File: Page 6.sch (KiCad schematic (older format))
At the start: 3 parts, among them U601 BME280

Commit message: Updates
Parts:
- C601, C602: Mftr Part No. (none) -> Yageo CC0603KPX7R7BB104
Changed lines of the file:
@@
 F 2 "Capacitor_SMD:C_0603_1608Metric_Pad1.05x0.95mm_HandSolder" H 7838 3700 50  0001 C CNN
 F 3 "https://www.yageo.com/upload/media/product/productsearch/datasheet/mlcc/UPY-GPHC_X7R_6.3V-to-50V_18.pdf" H 7800 3850 50  0001 C CNN
+F 4 "Yageo CC0603KPX7R7BB104" H 7800 3850 50  0001 C CNN "Mftr Part No."
 	1    7800 3850
 	1    0    0    -1
@@
 F 2 "Capacitor_SMD:C_0603_1608Metric_Pad1.05x0.95mm_HandSolder" H 7338 3700 50  0001 C CNN
 F 3 "https://www.yageo.com/upload/media/product/productsearch/datasheet/mlcc/UPY-GPHC_X7R_6.3V-to-50V_18.pdf" H 7300 3850 50  0001 C CNN
+F 4 "Yageo CC0603KPX7R7BB104" H 7300 3850 50  0001 C CNN "Mftr Part No."
 	1    7300 3850
 	1    0    0    -1

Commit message: Updates
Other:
- note added: "Environmental Sensor"
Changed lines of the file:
@@
 Wire Wire Line
 	7800 4000 7800 4650
+Text Notes 5750 5250 0    98   ~ 20
+Environmental Sensor
 $EndSCHEMATC

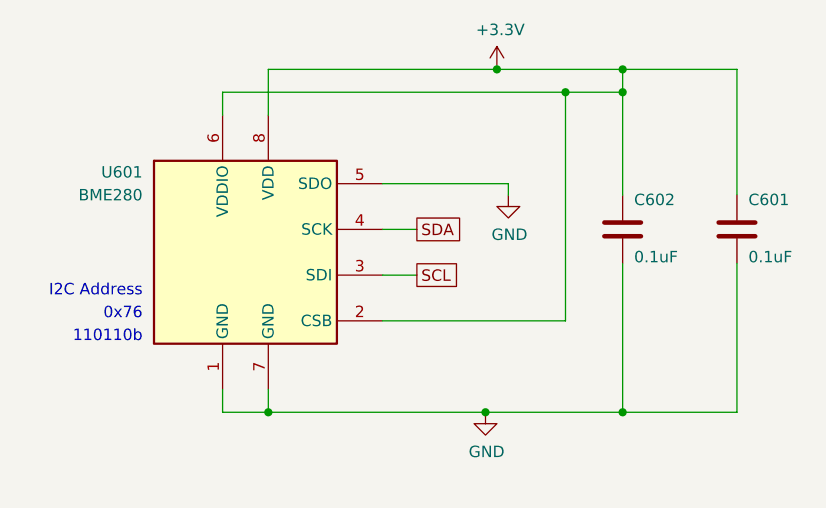
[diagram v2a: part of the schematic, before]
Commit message: Switched to Hierarchical
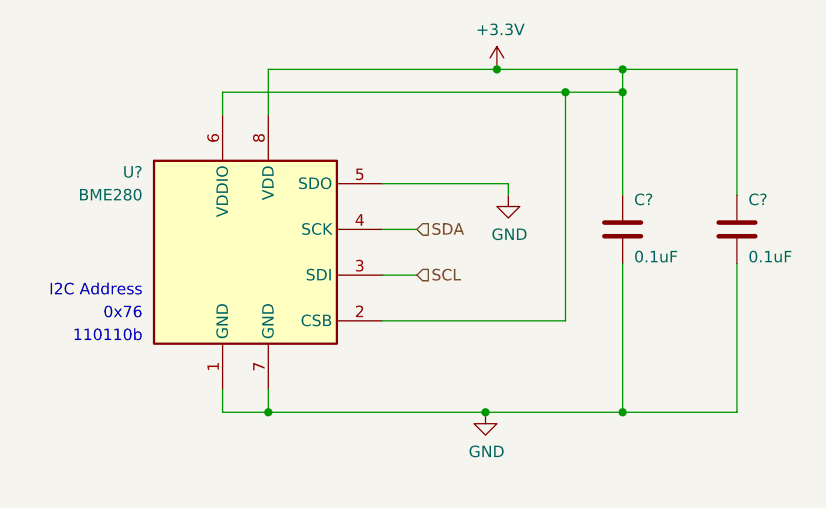
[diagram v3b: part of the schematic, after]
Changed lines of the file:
@@
 Comment4 ""
 $EndDescr
-Text GLabel 6400 3850 2    50   UnSpc ~ 0
-SDA
-Text GLabel 6400 4050 2    50   UnSpc ~ 0
-SCL
 Wire Wire Line
 	6250 3850 6400 3850
@@
 U 1 1 5EB1A0DE
 P 6800 3700
-F 0 "#PWR011" H 6800 3450 50  0001 C CNN
+F 0 "#PWR?" H 6800 3450 50  0001 C CNN
 F 1 "GND" H 6805 3527 50  0000 C CNN
 F 2 "" H 6800 3700 50  0001 C CNN
@@
 U 1 1 5EB1ABBF
 P 6700 4650
-F 0 "#PWR09" H 6700 4400 50  0001 C CNN
+F 0 "#PWR?" H 6700 4400 50  0001 C CNN
 F 1 "GND" H 6705 4477 50  0000 C CNN
 F 2 "" H 6700 4650 50  0001 C CNN
@@
 U 1 1 5EB22FF1
 P 6750 3150
-F 0 "#PWR010" H 6750 3000 50  0001 C CNN
+F 0 "#PWR?" H 6750 3000 50  0001 C CNN
 F 1 "+3.3V" H 6765 3323 50  0000 C CNN
 F 2 "" H 6750 3150 50  0001 C CNN
@@
 AR Path="/5EACA483/5EB22067" Ref="C?"  Part="1"
 AR Path="/5ECF3070/5EB22067" Ref="C601"  Part="1"
-F 0 "C601" H 7850 3950 50  0000 L BNN
+F 0 "C?" H 7850 3950 50  0000 L BNN
 F 1 "0.1uF" H 7850 3700 50  0000 L BNN
 F 2 "Capacitor_SMD:C_0603_1608Metric_Pad1.05x0.95mm_HandSolder" H 7838 3700 50  0001 C CNN
@@
 AR Path="/5EACA483/5EB21CE5" Ref="C?"  Part="1"
 AR Path="/5ECF3070/5EB21CE5" Ref="C602"  Part="1"
-F 0 "C602" H 7350 3950 50  0000 L BNN
+F 0 "C?" H 7350 3950 50  0000 L BNN
 F 1 "0.1uF" H 7350 3700 50  0000 L BNN
 F 2 "Capacitor_SMD:C_0603_1608Metric_Pad1.05x0.95mm_HandSolder" H 7338 3700 50  0001 C CNN
@@
 U 1 1 5EB18508
 P 5650 3950
-F 0 "U601" H 5200 4300 50  0000 R CNN
+F 0 "U?" H 5200 4300 50  0000 R CNN
 F 1 "BME280" H 5200 4200 50  0000 R CNN
 F 2 "Package_LGA:Bosch_LGA-8_2.5x2.5mm_P0.65mm_ClockwisePinNumbering" H 7150 3500 50  0001 C CNN
@@
 Text Notes 5750 5250 0    98   ~ 20
 Environmental Sensor
+Text HLabel 6400 3850 2    50   Input ~ 0
+SDA
+Text HLabel 6400 4050 2    50   Input ~ 0
+SCL
 $EndSCHEMATC

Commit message: Updating to Final Revision
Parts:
- added C601, C604: 0.1uF, Capacitor_SMD:C_0603_1608Metric_Pad1.05x0.95mm_HandSolder, symbol Device:C
- added C602: 6.8nF, Capacitor_SMD:C_0603_1608Metric_Pad1.05x0.95mm_HandSolder, symbol Device:C
- added C603: 0.12uF, Capacitor_SMD:C_0805_2012Metric_Pad1.15x1.40mm_HandSolder, symbol Device:C
- added C607, C608: 10pF, Capacitor_SMD:C_0603_1608Metric_Pad1.05x0.95mm_HandSolder, symbol Device:C
- added R601, R602: R10K0, Resistor_SMD:R_0603_1608Metric_Pad1.05x0.95mm_HandSolder, symbol Device:R
- added TP601: TP_nRST, Connector_Wire:SolderWirePad_1x01_SMD_5x10mm, symbol Connector:TestPoint
- added TP602: TP_IMU_INT, Connector_Wire:SolderWirePad_1x01_SMD_5x10mm, symbol Connector:TestPoint
- added TP603: TP_SDA, Connector_Wire:SolderWirePad_1x01_SMD_5x10mm, symbol Connector:TestPoint
- added TP604: TP_SCL, Connector_Wire:SolderWirePad_1x01_SMD_5x10mm, symbol Connector:TestPoint
- added U?: BNO055, Package_LGA:LGA-28_5.2x3.8mm_P0.5mm, symbol Sensor_Motion:BNO055
- added Y601: 32.7680 kHz, Name Plate Class Project:Oscillator_MC-405_32.7680K-D__ROHS, symbol Name~Plate~Class~Library:Oscillator_MC-405_32.7680K-D__ROHS
- renumbered C602 to C605, C601 to C606
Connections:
- net labels added: BNO055_INT, BNO055_SCL, BNO055_SDA, BNO055_nRST, IMU_INT
- wire segments 24 -> 94
- no-connect marks 0 -> 1
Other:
- note added: "Inertial Measurement Unit"
- moved on the sheet: C605, C606, U601

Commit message: Updates
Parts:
- R601, R602: value R10K0 -> 10K0; Manufacturer (none) -> Yageo
- TP601: value TP_nRST -> Test Point; Name (none) -> TP_nRST
- TP602: value TP_IMU_INT -> Test Point; Name (none) -> TP_IMU_INT
- TP603: value TP_SDA -> Test Point; Name (none) -> TP_SDA
- TP604: value TP_SCL -> Test Point; Name (none) -> TP_SCL
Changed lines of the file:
@@
 AR Path="/5ECF3070/5ED1C8D7" Ref="TP604"  Part="1"
 F 0 "TP604" H 2000 3750 50  0000 R CNN
-F 1 "TP_SCL" H 2000 3850 50  0000 R CNN
+F 1 "Test Point" H 2000 3850 50  0000 R CNN
 F 2 "Connector_Wire:SolderWirePad_1x01_SMD_5x10mm" H 2250 3700 50  0001 C CNN
-F 3 "~" H 2250 3700 50  0001 C CNN
+F 3 "None" H 2250 3700 50  0001 C CNN
+F 4 "TP_SCL" H 2050 3700 50  0001 C CNN "Name"
 	1    2050 3700
 	-1   0    0    1
@@
 AR Path="/5ECF3070/5ED1C8DF" Ref="TP603"  Part="1"
 F 0 "TP603" H 2100 3750 50  0000 L CNN
-F 1 "TP_SDA" H 2100 3650 50  0000 L CNN
+F 1 "Test Point" H 2100 3650 50  0000 L CNN
 F 2 "Connector_Wire:SolderWirePad_1x01_SMD_5x10mm" H 2250 3600 50  0001 C CNN
-F 3 "~" H 2250 3600 50  0001 C CNN
+F 3 "None" H 2250 3600 50  0001 C CNN
+F 4 "TP_SDA" H 2050 3600 50  0001 C CNN "Name"
 	1    2050 3600
 	1    0    0    -1
@@
 AR Path="/5ECF3070/5ED1C8EB" Ref="R602"  Part="1"
 F 0 "R602" H 1570 2746 50  0000 L CNN
-F 1 "R10K0" H 1570 2655 50  0000 L CNN
+F 1 "10K0" H 1570 2655 50  0000 L CNN
 F 2 "Resistor_SMD:R_0603_1608Metric_Pad1.05x0.95mm_HandSolder" V 1430 2700 50  0001 C CNN
 F 3 "https://www.yageo.com/upload/media/product/productsearch/datasheet/rchip/PYu-RC_Group_51_RoHS_L_10.pdf" H 1500 2700 50  0001 C CNN
 F 4 "311-10KGRCT-ND" H 1500 2700 50  0001 C CNN "DigiKey Part No."
 F 5 "Yageo RC0603JR-0710KL" H 1500 2700 50  0001 C CNN "Mftr Part No."
+F 6 "Yageo" H 1500 2700 50  0001 C CNN "Manufacturer"
 	1    1500 2700
 	1    0    0    -1
@@
 AR Path="/5ECF3070/5ED1C8F1" Ref="TP602"  Part="1"
 F 0 "TP602" H 2100 3250 50  0000 L CNN
-F 1 "TP_IMU_INT" H 2100 3150 50  0000 L CNN
+F 1 "Test Point" H 2100 3150 50  0000 L CNN
 F 2 "Connector_Wire:SolderWirePad_1x01_SMD_5x10mm" H 2250 3100 50  0001 C CNN
-F 3 "~" H 2250 3100 50  0001 C CNN
+F 3 "None" H 2250 3100 50  0001 C CNN
+F 4 "TP_IMU_INT" H 2050 3100 50  0001 C CNN "Name"
 	1    2050 3100
 	1    0    0    -1
@@
 AR Path="/5ECF3070/5ED1C8FC" Ref="R601"  Part="1"
 F 0 "R601" H 1070 2746 50  0000 L CNN
-F 1 "R10K0" H 1070 2655 50  0000 L CNN
+F 1 "10K0" H 1070 2655 50  0000 L CNN
 F 2 "Resistor_SMD:R_0603_1608Metric_Pad1.05x0.95mm_HandSolder" V 930 2700 50  0001 C CNN
 F 3 "https://www.yageo.com/upload/media/product/productsearch/datasheet/rchip/PYu-RC_Group_51_RoHS_L_10.pdf" H 1000 2700 50  0001 C CNN
 F 4 "311-10KGRCT-ND" H 1000 2700 50  0001 C CNN "DigiKey Part No."
 F 5 "Yageo RC0603JR-0710KL" H 1000 2700 50  0001 C CNN "Mftr Part No."
+F 6 "Yageo" H 1000 2700 50  0001 C CNN "Manufacturer"
 	1    1000 2700
 	1    0    0    -1
@@
 AR Path="/5ECF3070/5ED1C902" Ref="TP601"  Part="1"
 F 0 "TP601" H 2100 3050 50  0000 L CNN
-F 1 "TP_nRST" H 2100 2950 50  0000 L CNN
+F 1 "Test Point" H 2100 2950 50  0000 L CNN
 F 2 "Connector_Wire:SolderWirePad_1x01_SMD_5x10mm" H 2250 2900 50  0001 C CNN
-F 3 "~" H 2250 2900 50  0001 C CNN
+F 3 "None" H 2250 2900 50  0001 C CNN
+F 4 "TP_nRST" H 2050 2900 50  0001 C CNN "Name"
 	1    2050 2900
 	1    0    0    -1

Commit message: Updates to schematic
Switching to ATMega34UF chip.
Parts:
- C601, C604, C605, C606: DigiKey Part No. (none) -> 311-1335-1-ND; Manufacturer (none) -> Yageo; Mftr Part No. Yageo CC0603KPX7R7BB104 -> CC0603KPX7R7BB104
- C602: DigiKey Part No. (none) -> 732-7932-1-ND; Manufacturer (none) -> Wurth; Mftr Part No. Yageo CC0603KPX7R7BB104 -> CAPC160X80X92L35
- C603: DigiKey Part No. (none) -> 478-5161-1-ND; Manufacturer (none) -> AVX; Mftr Part No. AVX 08053C124KAT2A -> 08053C124KAT2A
- C607, C608: Manufacturer (none) -> Kemet; Mftr Part No. Kemet C0603C100J1GACTU -> C0603C100J1GACTU
- R601, R602: value 10K0 -> 10k; Mftr Part No. Yageo RC0603JR-0710KL -> RC0603JR-0710KL
- TP601, TP602, TP603, TP604: symbol Connector:TestPoint -> Name~Plate~Class~Library:TestPoint; DigiKey Part No. (none) -> None; Manufacturer (none) -> None; Mftr Part No. (none) -> None
- U601: renamed from U?; DigiKey Part No. (none) -> 828-1058-1-ND; Manufacturer (none) -> Bosch-Sensortec; Mftr Part No. (none) -> BOSCH_BNO055
- U602: renamed from U601; DigiKey Part No. (none) -> 828-1063-1-ND; Manufacturer (none) -> Bosch-Sensortec; Mftr Part No. (none) -> BOSCH_BME280
- Y601: DigiKey Part No. (none) -> SER4311TR-ND; Manufacturer (none) -> Epson; Mftr Part No. (none) -> MC-405 32.7680K-E3: ROHS

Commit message: Updates
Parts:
- C603: footprint Capacitor_SMD:C_0805_2012Metric_Pad1.15x1.40mm_HandSolder -> Capacitor_SMD:C_0805_2012Metric_HandSolder
- TP601, TP602, TP603, TP604: symbol Name~Plate~Class~Library:TestPoint -> Name_Plate_Class_Project:TestPoint
- Y601: footprint Name Plate Class Project:Oscillator_MC-405_32.7680K-D__ROHS -> Name_Plate_Class_Project:Oscillator_MC-405_32.7680K-D__ROHS; symbol Name~Plate~Class~Library:Oscillator_MC-405_32.7680K-D__ROHS -> Name_Plate_Class_Project:Oscillator_MC-405_32.7680K-D__ROHS
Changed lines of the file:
@@
 $EndComp
 $Comp
-L Name~Plate~Class~Library:Oscillator_MC-405_32.7680K-D__ROHS Y?
+L Name_Plate_Class_Project:Oscillator_MC-405_32.7680K-D__ROHS Y?
 U 1 1 5ED1C899
 P 4950 3150
@@
 F 0 "Y601" H 4850 3000 50  0000 L CNN
 F 1 "32.7680 kHz" H 4700 3300 50  0000 L CNN
-F 2 "Name Plate Class Project:Oscillator_MC-405_32.7680K-D__ROHS" H 4850 2850 50  0001 L BNN
+F 2 "Name_Plate_Class_Project:Oscillator_MC-405_32.7680K-D__ROHS" H 4850 2850 50  0001 L BNN
 F 3 "https://support.epson.biz/td/api/doc_check.php?dl=brief_MC-405&lang=en" H 4850 2750 50  0001 L BNN
 F 4 "SER4311TR-ND" H 4950 3150 50  0001 C CNN "DigiKey Part No."
@@
 F 0 "C603" H 5300 2150 50  0000 L BNN
 F 1 "0.12uF" H 5300 1900 50  0000 L BNN
-F 2 "Capacitor_SMD:C_0805_2012Metric_Pad1.15x1.40mm_HandSolder" H 5288 1900 50  0001 C CNN
+F 2 "Capacitor_SMD:C_0805_2012Metric_HandSolder" H 5288 1900 50  0001 C CNN
 F 3 "http://datasheets.avx.com/X7RDielectric.pdf" H 5250 2050 50  0001 C CNN
 F 4 "08053C124KAT2A" H 5250 2050 50  0001 C CNN "Mftr Part No."
@@
 	3250 2900 2050 2900
 $Comp
-L Name~Plate~Class~Library:TestPoint TP?
+L Name_Plate_Class_Project:TestPoint TP?
 U 1 1 5ED1C8D7
 P 2050 3700
@@
 AR Path="/5ECF3158/5ED1C8D7" Ref="TP?"  Part="1"
 AR Path="/5ECF3070/5ED1C8D7" Ref="TP604"  Part="1"
+AR Path="/5ED1C8D7" Ref="TP604"  Part="1"
 F 0 "TP604" H 2000 3750 50  0000 R CNN
 F 1 "Test Point" H 2000 3850 50  0001 R CNN
@@
 	2050 3700 1850 3700
 $Comp
-L Name~Plate~Class~Library:TestPoint TP?
+L Name_Plate_Class_Project:TestPoint TP?
 U 1 1 5ED1C8DF
 P 2050 3600
@@
 AR Path="/5ECF3158/5ED1C8DF" Ref="TP?"  Part="1"
 AR Path="/5ECF3070/5ED1C8DF" Ref="TP603"  Part="1"
+AR Path="/5ED1C8DF" Ref="TP603"  Part="1"
 F 0 "TP603" H 2100 3750 50  0000 L CNN
 F 1 "Test Point" H 2100 3650 50  0001 L CNN
@@
 $EndComp
 $Comp
-L Name~Plate~Class~Library:TestPoint TP?
+L Name_Plate_Class_Project:TestPoint TP?
 U 1 1 5ED1C8F1
 P 2050 3100
@@
 AR Path="/5ECF3158/5ED1C8F1" Ref="TP?"  Part="1"
 AR Path="/5ECF3070/5ED1C8F1" Ref="TP602"  Part="1"
+AR Path="/5ED1C8F1" Ref="TP602"  Part="1"
 F 0 "TP602" H 2100 3250 50  0000 L CNN
 F 1 "Test Point" H 2100 3150 50  0001 L CNN
@@
 $EndComp
 $Comp
-L Name~Plate~Class~Library:TestPoint TP?
+L Name_Plate_Class_Project:TestPoint TP?
 U 1 1 5ED1C902
 P 2050 2900
@@
 AR Path="/5ECF3158/5ED1C902" Ref="TP?"  Part="1"
 AR Path="/5ECF3070/5ED1C902" Ref="TP601"  Part="1"
+AR Path="/5ED1C902" Ref="TP601"  Part="1"
 F 0 "TP601" H 2100 3050 50  0000 L CNN
 F 1 "Test Point" H 2100 2950 50  0001 L CNN
